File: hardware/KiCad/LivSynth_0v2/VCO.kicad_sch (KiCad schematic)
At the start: 26 parts, among them J12 Jumper, J13 Jumper, J15 Jumper, Q12 2N3904, Q13 2N3904, Q14 2N3904, SW1 SW_SPDT, U4 TL074, U8 TL074

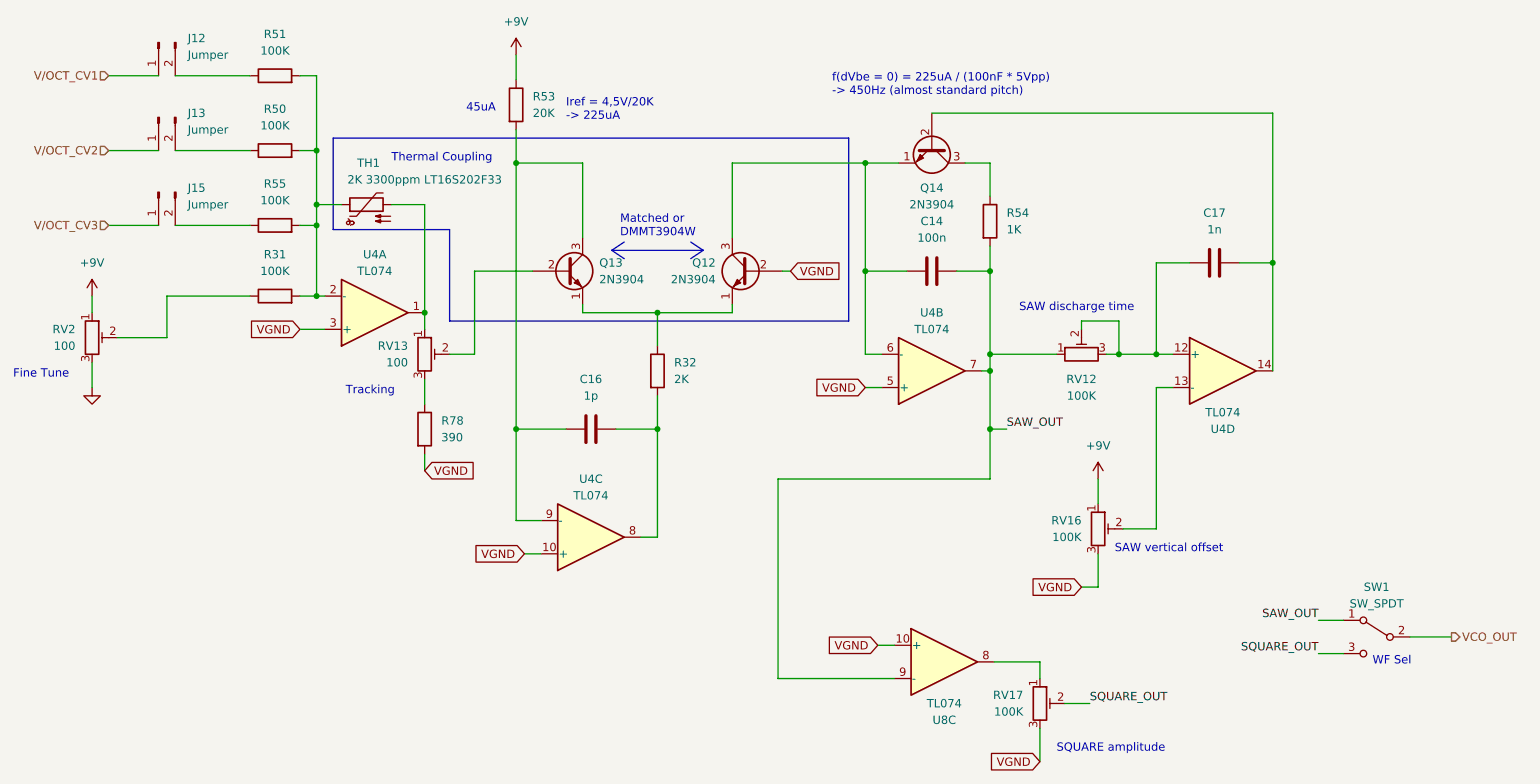
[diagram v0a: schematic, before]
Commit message: Analog redesign:  - Power: Add voltage and current test points  - MCU: use PA11/PA12 for USB DFU interface  - MCU: add NRST reset switch  - Slew: increase portamento cap  - VCO: invert trim pots  - VCF: let resonance kick in earlier  - VCF: invert pots  - VCA: invert trim pot  - EG: full redesign, properly referencing VGND now  - LFO: R61 = 51K  - ModMatrix: add EG attenuverters  - IO: invert pots  - IO: limit output gain for 1W speaker  - IO: connect BTN_SHIFT in gap free order to SR
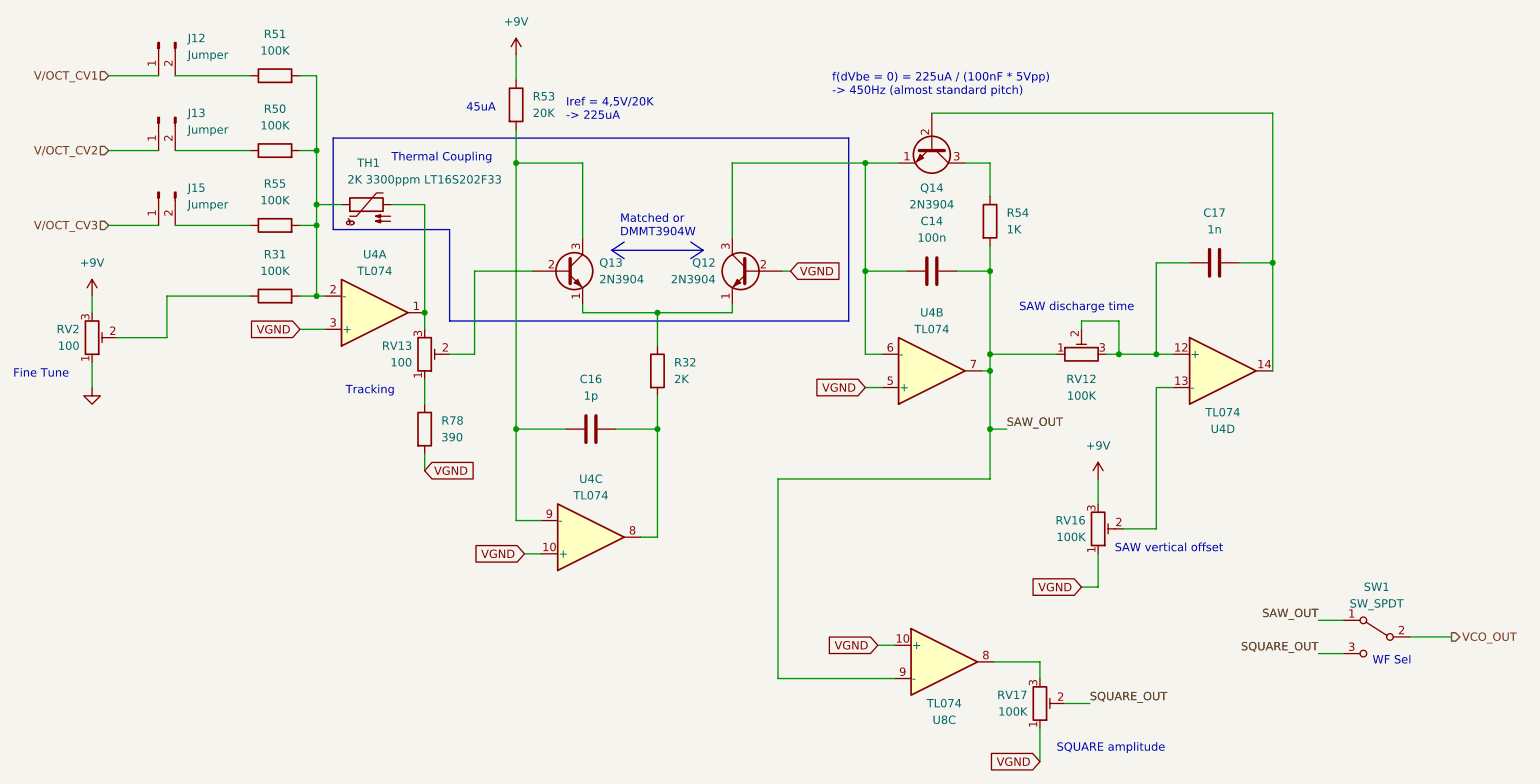
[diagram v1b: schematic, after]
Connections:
- net +9V: now also RV16.3, RV2.3; no longer RV16.1, RV2.1
- net GND: now also RV2.1; no longer RV2.3
- net VGND: now also RV16.1, RV17.1; no longer RV16.3, RV17.3
- net at TH1.2, U4.1: now also RV13.3; no longer RV13.1
- net at U8.8: now also RV17.3; no longer RV17.1
- net at R78.1: now also RV13.1; no longer RV13.3
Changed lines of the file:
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@@
     (pin "2")
   )
-  (symbol (lib_id "Device:R_Potentiometer_Trim") (at 198.755 109.22 0) (unit 1)
-    (in_bom yes) (on_board yes) (fields_autoplaced)
-    (property "Reference" "RV16" (id 0) (at 196.215 107.9499 0)
-      (effects (font (size 1.27 1.27)) (justify right))
-    )
-    (property "Value" "100K" (id 1) (at 196.215 110.4899 0)
+  (symbol (lib_id "Device:R_Potentiometer_Trim") (at 198.755 109.22 0) (mirror x) (unit 1)
+    (in_bom yes) (on_board yes) (fields_autoplaced)
+    (property "Reference" "RV16" (id 0) (at 196.85 107.9499 0)
+      (effects (font (size 1.27 1.27)) (justify right))
+    )
+    (property "Value" "100K" (id 1) (at 196.85 110.4899 0)
       (effects (font (size 1.27 1.27)) (justify right))
     )
@@
     (pin "3")
   )
-  (symbol (lib_id "Device:R_Potentiometer_Trim") (at 95.885 82.55 0) (unit 1)
-    (in_bom yes) (on_board yes) (fields_autoplaced)
-    (property "Reference" "RV13" (id 0) (at 93.345 81.2799 0)
-      (effects (font (size 1.27 1.27)) (justify right))
-    )
-    (property "Value" "100" (id 1) (at 93.345 83.8199 0)
+  (symbol (lib_id "Device:R_Potentiometer_Trim") (at 95.885 82.55 0) (mirror x) (unit 1)
+    (in_bom yes) (on_board yes) (fields_autoplaced)
+    (property "Reference" "RV13" (id 0) (at 93.98 81.2799 0)
+      (effects (font (size 1.27 1.27)) (justify right))
+    )
+    (property "Value" "100" (id 1) (at 93.98 83.8199 0)
       (effects (font (size 1.27 1.27)) (justify right))
     )
@@
     (pin "2")
   )
-  (symbol (lib_id "Device:R_Potentiometer_Trim") (at 45.085 80.01 0) (unit 1)
-    (in_bom yes) (on_board yes) (fields_autoplaced)
-    (property "Reference" "RV2" (id 0) (at 42.545 78.7399 0)
-      (effects (font (size 1.27 1.27)) (justify right))
-    )
-    (property "Value" "100" (id 1) (at 42.545 81.2799 0)
+  (symbol (lib_id "Device:R_Potentiometer_Trim") (at 45.085 80.01 0) (mirror x) (unit 1)
+    (in_bom yes) (on_board yes) (fields_autoplaced)
+    (property "Reference" "RV2" (id 0) (at 43.18 78.7399 0)
+      (effects (font (size 1.27 1.27)) (justify right))
+    )
+    (property "Value" "100" (id 1) (at 43.18 81.2799 0)
       (effects (font (size 1.27 1.27)) (justify right))
     )
@@
     (pin "4")
   )
-  (symbol (lib_id "Device:R_Potentiometer_Trim") (at 189.865 135.89 0) (unit 1)
-    (in_bom yes) (on_board yes) (fields_autoplaced)
-    (property "Reference" "RV17" (id 0) (at 187.325 134.6199 0)
-      (effects (font (size 1.27 1.27)) (justify right))
-    )
-    (property "Value" "100K" (id 1) (at 187.325 137.1599 0)
-      (effects (font (size 1.27 1.27)) (justify right))
-    )
+  (symbol (lib_id "Device:R_Potentiometer_Trim") (at 189.865 135.89 0) (mirror x) (unit 1)
+    (in_bom yes) (on_board yes) (fields_autoplaced)
+    (property "Reference" "RV17" (id 0) (at 187.96 134.6199 0)
+      (effects (font (size 1.27 1.27)) (justify right))
+    )
+    (property "Value" "100K" (id 1) (at 187.96 137.1599 0)
+      (effects (font (size 1.27 1.27)) (justify right))
+    )

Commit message: Analog Redesign:  - Power: Build ververse polarity protection using P-Mosfet and Zener Diode      - (https://www.youtube.com/watch?v=Ltx4vovY5Z4 - 1:28)  - Power: Build adjustable buck regulator for 8-9V stable voltage source  - PCB: Add location for order number ("JLCJLCJLCJLC")  - General: Add Tooling Holes for PCB assembly  - PCB: check frontend component layout for symmetry  - VCF: fix sound issues  - PCB: Add SloBlo icon  - PCB: Add switch labels to front side  - EG: test new design  - MCU: Add some debug pins
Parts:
- U4, U8: LCSC (none) -> C2057504
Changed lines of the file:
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@@
+      (effects (font (size 1.27 1.27)) hide)
+    )
+    (property "LCSC" "C2057504" (id 4) (at 88.265 76.2 0)
       (effects (font (size 1.27 1.27)) hide)
     )
@@
       (effects (font (size 1.27 1.27)) hide)
     )
+    (property "LCSC" "C2057504" (id 4) (at 175.26 129.54 0)
+      (effects (font (size 1.27 1.27)) hide)
+    )
     (pin "1")
     (pin "2")
@@
       (effects (font (size 1.27 1.27)) hide)
     )
+    (property "LCSC" "C2057504" (id 4) (at 121.285 110.49 0)
+      (effects (font (size 1.27 1.27)) hide)
+    )
     (pin "1")
     (pin "2")
@@
       (effects (font (size 1.27 1.27)) hide)
     )
+    (property "LCSC" "C2057504" (id 4) (at 217.805 85.09 0)
+      (effects (font (size 1.27 1.27)) hide)
+    )
     (pin "1")
     (pin "2")
@@
       (effects (font (size 1.27 1.27)) hide)
     )
+    (property "LCSC" "C2057504" (id 4) (at 173.355 85.09 0)
+      (effects (font (size 1.27 1.27)) hide)
+    )

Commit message: progress 2023-01-21
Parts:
- renumbered U8 to U3
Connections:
- net SAW_OUT: now also U3.13 (-); no longer U3.9 (-)
- net VGND: now also U3.12 (+); no longer U3.10 (+)
- net at RV17.3: now also U3.14; no longer U3.8
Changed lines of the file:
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@@
     (pin "1")
   )
-  (symbol (lib_id "Amplifier_Operational:TL074") (at 175.26 129.54 0) (unit 3)
-    (in_bom yes) (on_board yes)
-    (property "Reference" "U8" (id 0) (at 175.26 138.43 0))
+  (symbol (lib_id "Amplifier_Operational:TL074") (at 175.26 129.54 0) (unit 4)
+    (in_bom yes) (on_board yes)
+    (property "Reference" "U3" (id 0) (at 175.26 138.43 0))
     (property "Value" "TL074" (id 1) (at 175.26 135.89 0))
     (property "Footprint" "Package_SO:SOIC-14_3.9x8.7mm_P1.27mm" (id 2) (at 173.99 127 0)
@@
       (effects (font (size 1.27 1.27)) (justify left) hide)
     )
-    (property "Datasheet" "https://www.thonk.co.uk/wp-content/uploads/Documents/Datasheets/Tempco/Akaneohm_Tempco.pdf" (id 3) (at 86.995 59.69 0)
-      (effects (font (size 1.27 1.27)) hide)
-    )
+    (property "Datasheet" "~" (id 3) (at 86.995 59.69 0)
+      (effects (font (size 1.27 1.27)) hide)
+    )

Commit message: Geographical reannotate
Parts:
- renumbered C16 to C11, C14 to C13, C17 to C5, J12 to J15, J13 to J16, J15 to J17, Q12 to Q11, Q13 to Q12, R31 to R22, R53 to R23, R32 to R36, R51 to R37, R50 to R38, R55 to R39, R54 to R48, R78 to R65, RV13 to RV12, RV12 to RV15, U4 to U2, U3 to U4
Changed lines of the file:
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@@
   (symbol (lib_id "Device:R") (at 73.025 62.865 90) (unit 1)
     (in_bom yes) (on_board yes) (fields_autoplaced)
-    (property "Reference" "R55" (id 0) (at 73.025 56.515 90))
+    (property "Reference" "R39" (id 0) (at 73.025 56.515 90))
     (property "Value" "100K" (id 1) (at 73.025 59.055 90))
     (property "Footprint" "Resistor_THT:R_Axial_DIN0207_L6.3mm_D2.5mm_P7.62mm_Horizontal" (id 2) (at 73.025 64.643 90)
@@
   (symbol (lib_id "Connector:Conn_01x02_Male") (at 55.245 46.355 90) (mirror x) (unit 1)
     (in_bom yes) (on_board yes) (fields_autoplaced)
-    (property "Reference" "J13" (id 0) (at 59.69 45.7199 90)
+    (property "Reference" "J16" (id 0) (at 59.69 45.7199 90)
       (effects (font (size 1.27 1.27)) (justify right))
     )
@@
   (symbol (lib_id "Device:R") (at 182.245 62.23 0) (unit 1)
     (in_bom yes) (on_board yes) (fields_autoplaced)
-    (property "Reference" "R54" (id 0) (at 184.785 60.9599 0)
+    (property "Reference" "R48" (id 0) (at 184.785 60.9599 0)
       (effects (font (size 1.27 1.27)) (justify left))
     )
@@
   (symbol (lib_id "Amplifier_Operational:TL074") (at 88.265 76.2 0) (mirror x) (unit 1)
     (in_bom yes) (on_board yes)
-    (property "Reference" "U4" (id 0) (at 88.265 67.31 0))
+    (property "Reference" "U2" (id 0) (at 88.265 67.31 0))
     (property "Value" "TL074" (id 1) (at 88.265 69.85 0))
     (property "Footprint" "Package_SO:SOIC-14_3.9x8.7mm_P1.27mm" (id 2) (at 86.995 78.74 0)
@@
   (symbol (lib_id "Device:R") (at 131.445 85.09 0) (unit 1)
     (in_bom yes) (on_board yes) (fields_autoplaced)
-    (property "Reference" "R32" (id 0) (at 133.985 83.8199 0)
+    (property "Reference" "R36" (id 0) (at 133.985 83.8199 0)
       (effects (font (size 1.27 1.27)) (justify left))
     )
@@
   (symbol (lib_id "Device:C") (at 121.285 93.98 90) (unit 1)
     (in_bom yes) (on_board yes) (fields_autoplaced)
-    (property "Reference" "C16" (id 0) (at 121.285 86.36 90))
+    (property "Reference" "C11" (id 0) (at 121.285 86.36 90))
     (property "Value" "1p" (id 1) (at 121.285 88.9 90))
     (property "Footprint" "Capacitor_THT:C_Disc_D3.0mm_W1.6mm_P2.50mm" (id 2) (at 125.095 93.0148 0)
@@
   (symbol (lib_id "Amplifier_Operational:TL074") (at 175.26 129.54 0) (unit 4)
     (in_bom yes) (on_board yes)
-    (property "Reference" "U3" (id 0) (at 175.26 138.43 0))
+    (property "Reference" "U4" (id 0) (at 175.26 138.43 0))
     (property "Value" "TL074" (id 1) (at 175.26 135.89 0))
     (property "Footprint" "Package_SO:SOIC-14_3.9x8.7mm_P1.27mm" (id 2) (at 173.99 127 0)
@@
   (symbol (lib_id "Device:R") (at 73.025 51.435 90) (unit 1)
     (in_bom yes) (on_board yes) (fields_autoplaced)
-    (property "Reference" "R50" (id 0) (at 73.025 45.085 90))
+    (property "Reference" "R38" (id 0) (at 73.025 45.085 90))
     (property "Value" "100K" (id 1) (at 73.025 47.625 90))
     (property "Footprint" "Resistor_THT:R_Axial_DIN0207_L6.3mm_D2.5mm_P7.62mm_Horizontal" (id 2) (at 73.025 53.213 90)
@@
   (symbol (lib_id "Transistor_BJT:2N3904") (at 145.415 69.85 0) (mirror y) (unit 1)
     (in_bom yes) (on_board yes) (fields_autoplaced)
-    (property "Reference" "Q12" (id 0) (at 140.335 68.5799 0)
+    (property "Reference" "Q11" (id 0) (at 140.335 68.5799 0)
       (effects (font (size 1.27 1.27)) (justify left))
     )
@@
   (symbol (lib_id "Device:R_Potentiometer_Trim") (at 95.885 82.55 0) (mirror x) (unit 1)
     (in_bom yes) (on_board yes) (fields_autoplaced)
-    (property "Reference" "RV13" (id 0) (at 93.98 81.2799 0)
+    (property "Reference" "RV12" (id 0) (at 93.98 81.2799 0)
       (effects (font (size 1.27 1.27)) (justify right))
     )
@@
   (symbol (lib_id "Device:R") (at 73.025 73.66 90) (unit 1)
     (in_bom yes) (on_board yes) (fields_autoplaced)
-    (property "Reference" "R31" (id 0) (at 73.025 67.31 90))
+    (property "Reference" "R22" (id 0) (at 73.025 67.31 90))
     (property "Value" "100K" (id 1) (at 73.025 69.85 90))
     (property "Footprint" "Resistor_THT:R_Axial_DIN0207_L6.3mm_D2.5mm_P7.62mm_Horizontal" (id 2) (at 73.025 75.438 90)
@@
   (symbol (lib_id "Device:C") (at 173.355 69.85 90) (unit 1)
     (in_bom yes) (on_board yes) (fields_autoplaced)
-    (property "Reference" "C14" (id 0) (at 173.355 62.23 90))
+    (property "Reference" "C13" (id 0) (at 173.355 62.23 90))
     (property "Value" "100n" (id 1) (at 173.355 64.77 90))
     (property "Footprint" "Capacitor_THT:C_Rect_L7.2mm_W2.5mm_P5.00mm_FKS2_FKP2_MKS2_MKP2" (id 2) (at 177.165 68.8848 0)
@@
   (symbol (lib_id "Connector:Conn_01x02_Male") (at 55.245 57.785 90) (mirror x) (unit 1)
     (in_bom yes) (on_board yes) (fields_autoplaced)
-    (property "Reference" "J15" (id 0) (at 59.69 57.1499 90)
+    (property "Reference" "J17" (id 0) (at 59.69 57.1499 90)
       (effects (font (size 1.27 1.27)) (justify right))
     )
@@
   (symbol (lib_id "Amplifier_Operational:TL074") (at 121.285 110.49 0) (mirror x) (unit 3)
     (in_bom yes) (on_board yes)
-    (property "Reference" "U4" (id 0) (at 121.285 101.6 0))
+    (property "Reference" "U2" (id 0) (at 121.285 101.6 0))
     (property "Value" "TL074" (id 1) (at 121.285 104.14 0))
     (property "Footprint" "Package_SO:SOIC-14_3.9x8.7mm_P1.27mm" (id 2) (at 120.015 113.03 0)
@@
   (symbol (lib_id "Device:R_Potentiometer_Trim") (at 196.215 82.55 90) (unit 1)
     (in_bom yes) (on_board yes) (fields_autoplaced)
-    (property "Reference" "RV12" (id 0) (at 196.215 86.36 90))
+    (property "Reference" "RV15" (id 0) (at 196.215 86.36 90))
     (property "Value" "100K" (id 1) (at 196.215 88.9 90))
     (property "Footprint" "SloBlo:Potentiometer_Bourns_3296W_Vertical" (id 2) (at 196.215 82.55 0)
@@
   (symbol (lib_id "Device:C") (at 216.535 68.58 90) (unit 1)
     (in_bom yes) (on_board yes) (fields_autoplaced)
-    (property "Reference" "C17" (id 0) (at 216.535 60.96 90))
+    (property "Reference" "C5" (id 0) (at 216.535 60.96 90))
     (property "Value" "1n" (id 1) (at 216.535 63.5 90))
     (property "Footprint" "Capacitor_THT:C_Rect_L7.2mm_W2.5mm_P5.00mm_FKS2_FKP2_MKS2_MKP2" (id 2) (at 220.345 67.6148 0)
@@
   (symbol (lib_id "Amplifier_Operational:TL074") (at 217.805 85.09 0) (unit 4)
     (in_bom yes) (on_board yes)
-    (property "Reference" "U4" (id 0) (at 217.805 93.98 0))
+    (property "Reference" "U2" (id 0) (at 217.805 93.98 0))
     (property "Value" "TL074" (id 1) (at 217.805 91.44 0))
     (property "Footprint" "Package_SO:SOIC-14_3.9x8.7mm_P1.27mm" (id 2) (at 216.535 82.55 0)
@@
   (symbol (lib_id "Connector:Conn_01x02_Male") (at 55.245 34.925 90) (mirror x) (unit 1)
     (in_bom yes) (on_board yes) (fields_autoplaced)
-    (property "Reference" "J12" (id 0) (at 59.69 34.2899 90)
+    (property "Reference" "J15" (id 0) (at 59.69 34.2899 90)
       (effects (font (size 1.27 1.27)) (justify right))
     )
@@
   (symbol (lib_id "Device:R") (at 73.025 40.005 90) (unit 1)
     (in_bom yes) (on_board yes) (fields_autoplaced)
-    (property "Reference" "R51" (id 0) (at 73.025 33.655 90))
+    (property "Reference" "R37" (id 0) (at 73.025 33.655 90))
     (property "Value" "100K" (id 1) (at 73.025 36.195 90))
     (property "Footprint" "Resistor_THT:R_Axial_DIN0207_L6.3mm_D2.5mm_P7.62mm_Horizontal" (id 2) (at 73.025 41.783 90)
@@
   (symbol (lib_id "Transistor_BJT:2N3904") (at 117.475 69.85 0) (unit 1)
     (in_bom yes) (on_board yes) (fields_autoplaced)
-    (property "Reference" "Q13" (id 0) (at 122.555 68.5799 0)
+    (property "Reference" "Q12" (id 0) (at 122.555 68.5799 0)
       (effects (font (size 1.27 1.27)) (justify left))
     )
@@
   (symbol (lib_id "Device:R") (at 95.885 93.98 0) (unit 1)
     (in_bom yes) (on_board yes) (fields_autoplaced)
-    (property "Reference" "R78" (id 0) (at 98.425 92.7099 0)
+    (property "Reference" "R65" (id 0) (at 98.425 92.7099 0)
       (effects (font (size 1.27 1.27)) (justify left))
     )
@@
   (symbol (lib_id "Device:R") (at 109.855 44.45 0) (unit 1)
     (in_bom yes) (on_board yes)
-    (property "Reference" "R53" (id 0) (at 112.395 43.1799 0)
+    (property "Reference" "R23" (id 0) (at 112.395 43.1799 0)
       (effects (font (size 1.27 1.27)) (justify left))
     )
@@
   (symbol (lib_id "Amplifier_Operational:TL074") (at 173.355 85.09 0) (mirror x) (unit 2)
     (in_bom yes) (on_board yes)
-    (property "Reference" "U4" (id 0) (at 173.355 76.2 0))
+    (property "Reference" "U2" (id 0) (at 173.355 76.2 0))
     (property "Value" "TL074" (id 1) (at 173.355 78.74 0))
     (property "Footprint" "Package_SO:SOIC-14_3.9x8.7mm_P1.27mm" (id 2) (at 172.085 87.63 0)

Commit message: Modify toggle switches (footprint and 3D model) Align R value designators Add JLC component placement checkup file
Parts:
- SW1: footprint SloBlo:SW_Toggle_MS500C -> SloBlo:SW_Toggle_MS500
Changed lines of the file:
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@@
     (property "Reference" "SW1" (id 0) (at 241.3 118.11 0))
     (property "Value" "SW_SPDT" (id 1) (at 241.3 120.65 0))
-    (property "Footprint" "SloBlo:SW_Toggle_MS500C" (id 2) (at 241.3 125.73 0)
+    (property "Footprint" "SloBlo:SW_Toggle_MS500" (id 2) (at 241.3 125.73 0)
       (effects (font (size 1.27 1.27)) hide)
     )

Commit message: Create new 0v3 folder
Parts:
- SW1: footprint SloBlo:SW_Toggle_MS500 -> SloBlo:SW_Toggle_MS500C
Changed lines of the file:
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@@
     (property "Reference" "SW1" (id 0) (at 241.3 118.11 0))
     (property "Value" "SW_SPDT" (id 1) (at 241.3 120.65 0))
-    (property "Footprint" "SloBlo:SW_Toggle_MS500" (id 2) (at 241.3 125.73 0)
+    (property "Footprint" "SloBlo:SW_Toggle_MS500C" (id 2) (at 241.3 125.73 0)
       (effects (font (size 1.27 1.27)) hide)
     )
